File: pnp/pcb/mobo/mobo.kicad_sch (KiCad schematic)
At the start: 38 parts, among them J1 SWD Header, SW1 SW_Push, SW2 SW_Push, U1 STM32F407VETx, Y1 8MHz

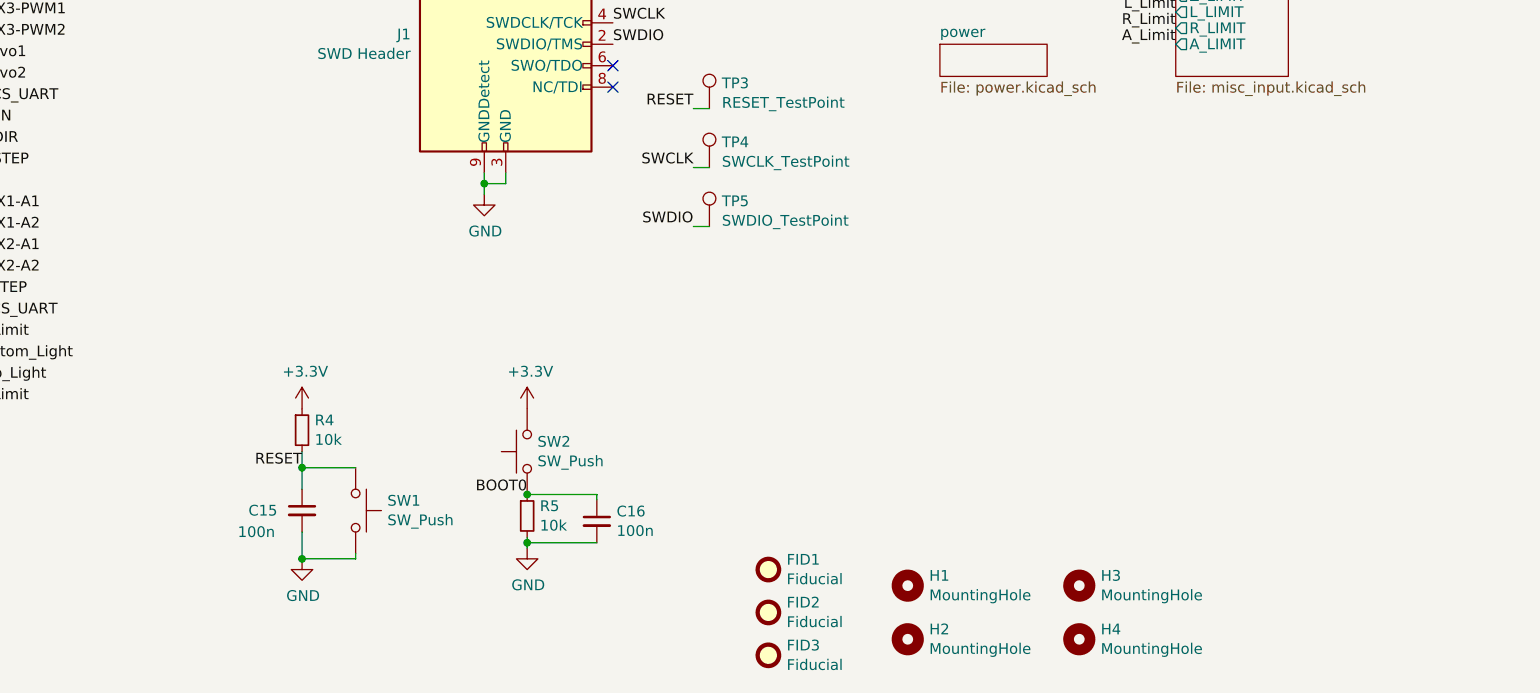
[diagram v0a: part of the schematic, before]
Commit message: Test version replacement in title block
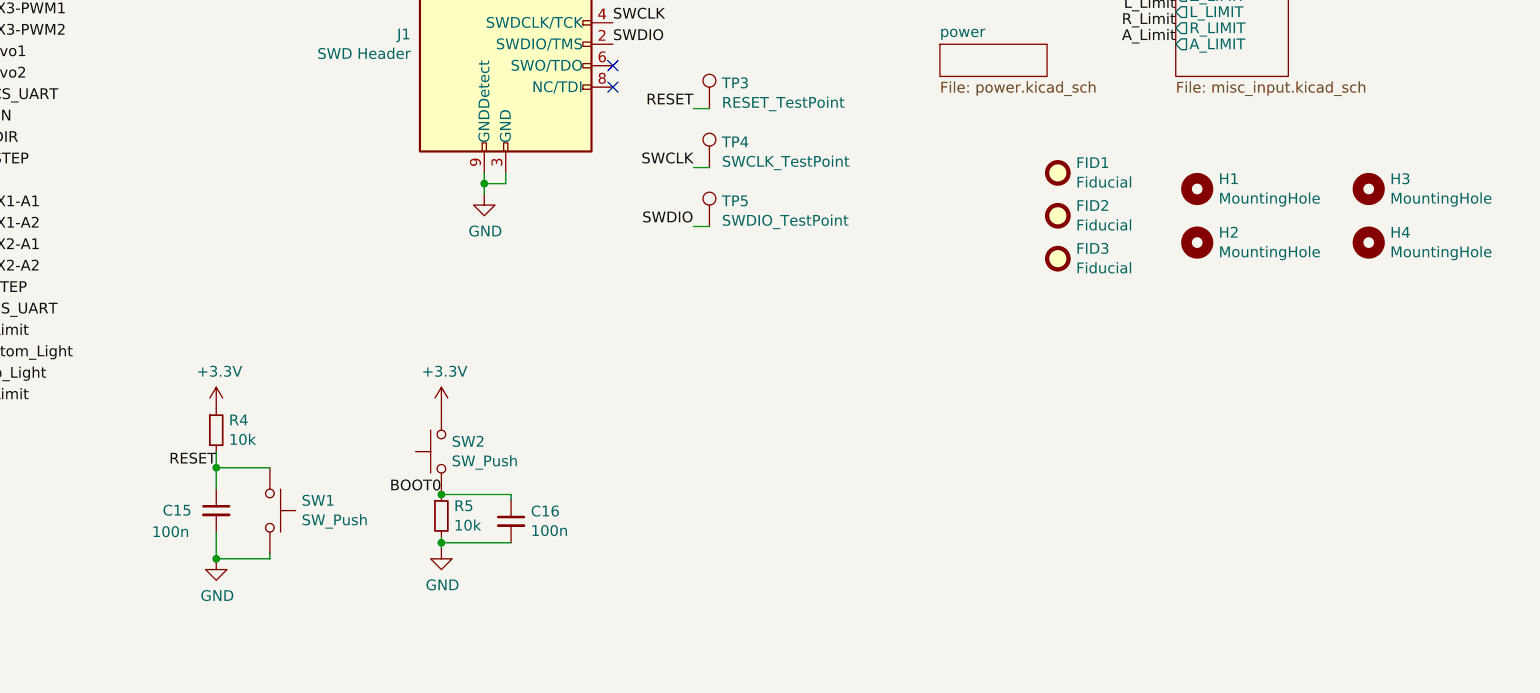
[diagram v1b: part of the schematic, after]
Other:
- moved on the sheet: C15, C16, FID1, FID2, FID3, H1, H2, H3, H4, R4, R5, SW1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

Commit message: Clean up, working
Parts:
- removed C1, C14, C3, C6, C7: 2.2u, Capacitor_SMD:C_0805_2012Metric, symbol Device:C_Small
- removed C10, C11, C12, C13, C15, C16, C8, C9: 100n, Capacitor_SMD:C_0805_2012Metric, symbol Device:C_Small
- removed C2, C4: 10p, Capacitor_SMD:C_0805_2012Metric, symbol Device:C_Small
- removed FB1: 2.5k, Inductor_SMD:L_0805_2012Metric, symbol Device:Ferrite_Bead
- removed FID1, FID2, FID3: Fiducial, Fiducial:Fiducial_1mm_Mask2mm, symbol Mechanical:Fiducial
- removed H1, H2, H3, H4: MountingHole, MountingHole:MountingHole_3.2mm_M3_DIN965_Pad, symbol Mechanical:MountingHole
- removed J1: SWD Header, Connector_PinHeader_1.27mm:PinHeader_2x05_P1.27mm_Vertical_SMD, symbol Connector:Conn_ARM_JTAG_SWD_10
- removed R1, R2: 4.7k, Resistor_SMD:R_0805_2012Metric, symbol Device:R_Small
- removed R3, R4, R5: 10k, Resistor_SMD:R_0805_2012Metric, symbol Device:R_Small
- removed SW1, SW2: SW_Push, Button_Switch_SMD:SW_SPST_B3S-1000, symbol Switch:SW_Push
- removed TP3: RESET_TestPoint, TestPoint:TestPoint_Pad_D2.0mm, symbol Connector:TestPoint
- removed TP4: SWCLK_TestPoint, TestPoint:TestPoint_Pad_D2.0mm, symbol Connector:TestPoint
- removed TP5: SWDIO_TestPoint, TestPoint:TestPoint_Pad_D2.0mm, symbol Connector:TestPoint
- removed TP6: BOOT0_TestPoint, TestPoint:TestPoint_Pad_D2.0mm, symbol Connector:TestPoint
- removed U1: STM32F407VETx, Package_QFP:LQFP-100_14x14mm_P0.5mm, symbol MCU_ST_STM32F4:STM32F407VETx
- removed Y1: 8MHz, Crystal:Crystal_SMD_3225-4Pin_3.2x2.5mm, symbol Device:Crystal_GND24_Small
- added J5: JST B8PS-VH, Connector_JST:JST_VH_B8PS-VH_1x08_P3.96mm_Horizontal, symbol Connector_Generic:Conn_01x08
- added J6: JST B5B-XH, Connector_JST:JST_XH_B5B-XH-A_1x05_P2.50mm_Vertical, symbol Connector_Generic:Conn_01x05
- C5: value 100n -> 100nF 50V; footprint Capacitor_SMD:C_0805_2012Metric -> Capacitor_SMD:C_0603_1608Metric; Digikey 1276-1180-1-ND -> (none); JLCPCB C49678 -> (none); LCSC C360619 -> (none); Manufacturer (none) -> Murata; Mouser 581-08055C104K -> (none); Partnumber (none) -> GCM188L81H104KA57D
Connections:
- net +3V3 is gone; now on net GND: C5.1
- net GND: now also J5.4 (Pin_4), J6.1 (Pin_1); no longer C5.2
- new net +5VP: C5.2, J5.8 (Pin_8), J6.5 (Pin_5)
- new net Driver/HU: J5.5 (Pin_5), J6.2 (Pin_2)
- new net Driver/HV: J5.6 (Pin_6), J6.3 (Pin_3)
- new net Driver/HW: J5.7 (Pin_7), J6.4 (Pin_4)
- new net Driver/U: J5.1 (Pin_1)
- new net Driver/V: J5.2 (Pin_2)
- new net Driver/W: J5.3 (Pin_3)
- no-connect marks 18 -> 0
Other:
- removed sheet misc_input
- removed sheet misc_output
- removed sheet motor_control
- removed sheet power
- removed sheet usb
- added sheet Driver (Driver.kicad_sch)
- added sheet Inputs (Inputs.kicad_sch)
- added sheet Miscellaneous (Misc.kicad_sch)
- added sheet Mosfets (Mosfets.kicad_sch)
- added sheet Power (Power.kicad_sch)
- note added: "- 24V input - 5V LDO - Power leds"
- note added: "- Mounting holes - Fiducials"
- note removed: "Analog Decoupling"
- note removed: "Digital Decoupling"
- company: (none) -> 3devo
- title: Index Mobo -> GD BLDC blower driver
